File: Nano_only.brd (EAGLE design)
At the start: 53 x 20.3 mm, 3 parts

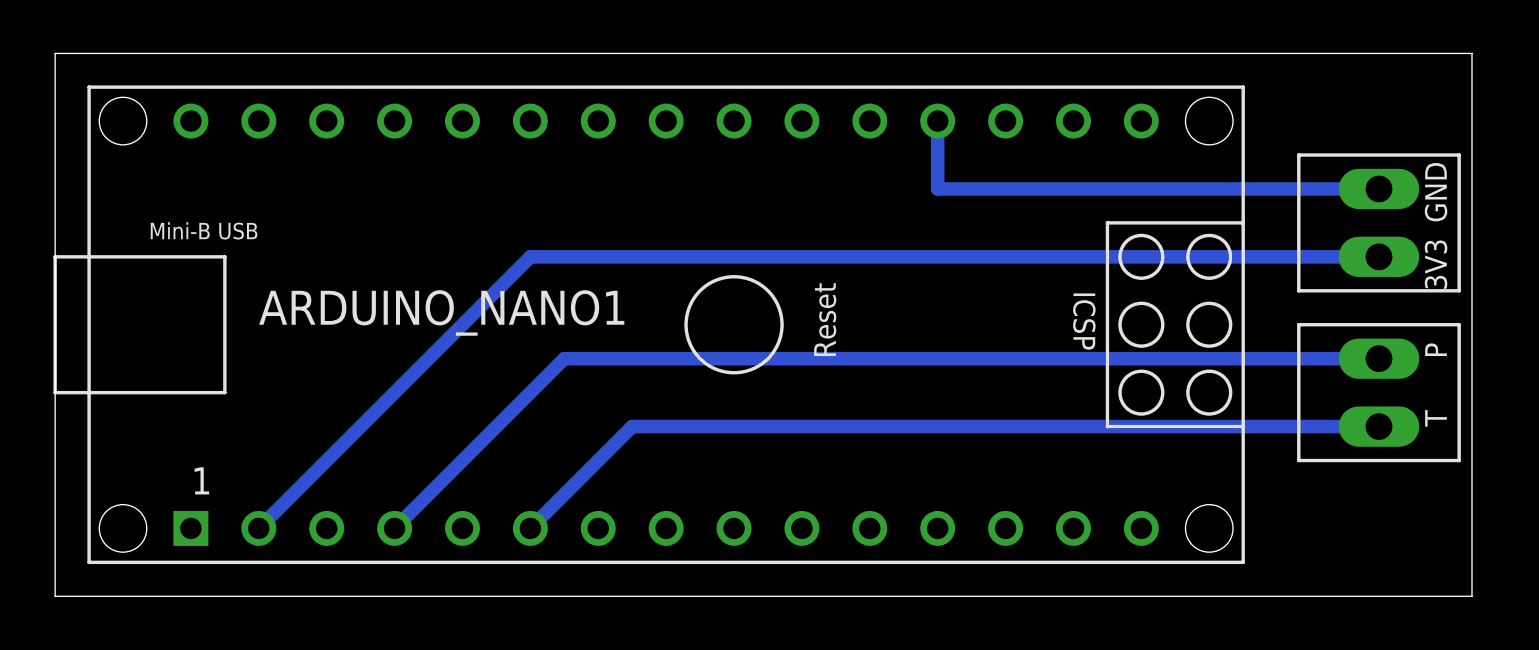
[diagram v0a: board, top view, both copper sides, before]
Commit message: Added some text on Nano_only.brd
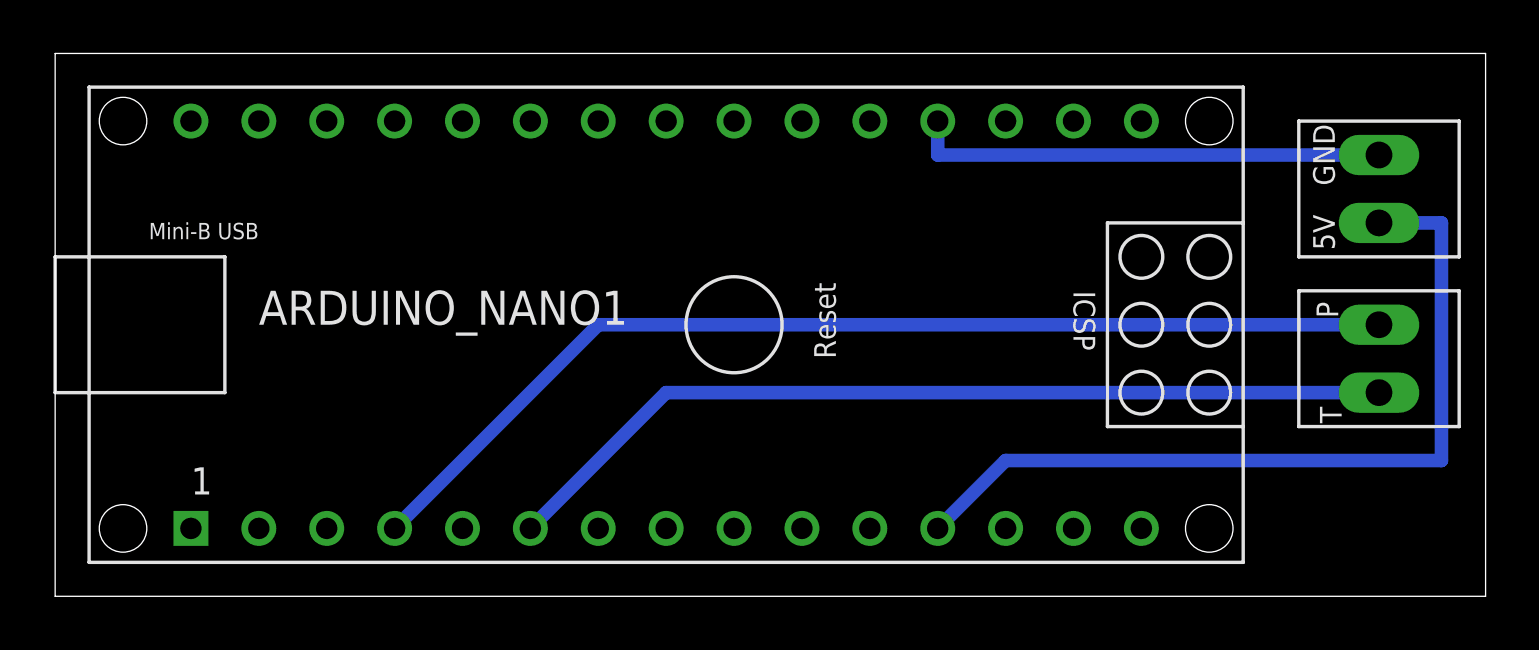
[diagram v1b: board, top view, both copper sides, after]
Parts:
- moved TPIN--PPIN 1.27 mm to (49.5, 8.89)
- moved 3.3V--GND 1.27 mm to (49.5, 15.2)
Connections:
- removed net 3V3: 3.3V--GND.P$1, ARDUINO_NANO1.2
- removed net 5V: ARDUINO_NANO1.12
- new net N$1: 3.3V--GND.P$1, ARDUINO_NANO1.12
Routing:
- net 3V3: track 46.1 -> 0.00 mm
- net N$1: track 0.00 -> 31.1 mm
- net GND: track 19.0 -> 17.8 mm
- net TPIN: track 33.3 -> 33.9 mm
- net PPIN: track 39.4 -> 39.9 mm
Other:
- board size 53 x 20.3 mm -> 53.5 x 20.3 mm
- board text added: "5V"
- board text removed: "3V3"
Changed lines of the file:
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@@
 <board>
 <plain>
-<wire x1="0" y1="0" x2="53.01" y2="0" width="0" layer="20"/>
-<wire x1="53.01" y1="0" x2="53.01" y2="20.31" width="0" layer="20"/>
-<wire x1="53.01" y1="20.31" x2="0" y2="20.31" width="0" layer="20"/>
+<wire x1="0" y1="0" x2="53.518" y2="0" width="0" layer="20"/>
+<wire x1="53.518" y1="0" x2="53.518" y2="20.31" width="0" layer="20"/>
+<wire x1="53.518" y1="20.31" x2="0" y2="20.31" width="0" layer="20"/>
 <wire x1="0" y1="20.31" x2="0" y2="0" width="0" layer="20"/>
-<text x="52.07" y="13.97" size="0.8128" layer="25" rot="R90">GND</text>
-<text x="52.07" y="11.43" size="0.8128" layer="25" rot="R90">3V3</text>
-<text x="52.07" y="8.89" size="0.8128" layer="25" rot="R90">P</text>
-<text x="52.07" y="6.35" size="0.8128" layer="25" rot="R90">T</text>
+<text x="47.879" y="15.367" size="0.8128" layer="25" rot="R90">GND</text>
+<text x="47.879" y="12.954" size="0.8128" layer="25" rot="R90">5V</text>
+<text x="48.006" y="10.414" size="0.8128" layer="25" rot="R90">P</text>
+<text x="48.133" y="6.477" size="0.8128" layer="25" rot="R90">T</text>
 </plain>
 <attributes>
@@
 </autorouter>
 <elements>
-<element name="3.3V--GND" library="johannes" package="CONRAD567588" value="CONRAD567588-2" x="49.53" y="13.97" smashed="yes" rot="R90"/>
+<element name="3.3V--GND" library="johannes" package="CONRAD567588" value="CONRAD567588-2" x="49.53" y="15.24" smashed="yes" rot="R90"/>
 <element name="ARDUINO_NANO1" library="ArduinoNanoV30" package="ARDUINO_NANO" value="" x="25.4" y="10.16" smashed="yes">
 <attribute name="NAME" x="7.62" y="10.16" size="1.27" layer="21" font="vector"/>
 <attribute name="VALUE" x="7.62" y="7.62" size="1.27" layer="21" font="vector"/>
 </element>
-<element name="TPIN--PPIN" library="johannes" package="CONRAD567588" value="CONRAD567588-2" x="49.53" y="7.62" smashed="yes" rot="R90"/>
+<element name="TPIN--PPIN" library="johannes" package="CONRAD567588" value="CONRAD567588-2" x="49.53" y="8.89" smashed="yes" rot="R90"/>
 </elements>
 <signals>
@@
 <contactref element="ARDUINO_NANO1" pad="14"/>
 <contactref element="ARDUINO_NANO1" pad="19"/>
-<wire x1="33.02" y1="17.78" x2="33.02" y2="15.24" width="0.508" layer="16"/>
-<wire x1="33.02" y1="15.24" x2="49.53" y2="15.24" width="0.508" layer="16"/>
+<wire x1="33.02" y1="17.78" x2="33.02" y2="16.51" width="0.508" layer="16"/>
+<wire x1="33.02" y1="16.51" x2="49.53" y2="16.51" width="0.508" layer="16"/>
 <wire x1="38.1" y1="2.54" x2="33.02" y2="17.78" width="0" layer="19" extent="1-1"/>
-</signal>
-<signal name="5V">
-<contactref element="ARDUINO_NANO1" pad="12"/>
 </signal>
 <signal name="VIN">
@@
 <contactref element="ARDUINO_NANO1" pad="6"/>
 <contactref element="TPIN--PPIN" pad="P$1"/>
-<wire x1="49.53" y1="6.35" x2="21.59" y2="6.35" width="0.508" layer="16"/>
-<wire x1="21.59" y1="6.35" x2="17.78" y2="2.54" width="0.508" layer="16"/>
+<wire x1="49.53" y1="7.62" x2="22.86" y2="7.62" width="0.508" layer="16"/>
+<wire x1="22.86" y1="7.62" x2="17.78" y2="2.54" width="0.508" layer="16"/>
 </signal>
 <signal name="PPIN">
 <contactref element="ARDUINO_NANO1" pad="4"/>
 <contactref element="TPIN--PPIN" pad="P$2"/>
-<wire x1="49.53" y1="8.89" x2="19.05" y2="8.89" width="0.508" layer="16"/>
-<wire x1="19.05" y1="8.89" x2="12.8016" y2="2.6416" width="0.508" layer="16"/>
+<wire x1="49.53" y1="10.16" x2="20.32" y2="10.16" width="0.508" layer="16"/>
+<wire x1="20.32" y1="10.16" x2="12.8016" y2="2.6416" width="0.508" layer="16"/>
 <wire x1="12.8016" y1="2.6416" x2="12.8016" y2="2.5908" width="0.254" layer="16"/>
 <wire x1="12.8016" y1="2.5908" x2="12.7" y2="2.54" width="0" layer="19" extent="16-16"/>
 </signal>
-<signal name="3V3">
+<signal name="N$1">
 <contactref element="3.3V--GND" pad="P$1"/>
-<contactref element="ARDUINO_NANO1" pad="2"/>
-<wire x1="49.53" y1="12.7" x2="17.78" y2="12.7" width="0.508" layer="16"/>
-<wire x1="17.78" y1="12.7" x2="7.62" y2="2.54" width="0.508" layer="16"/>
+<contactref element="ARDUINO_NANO1" pad="12"/>
+<wire x1="33.02" y1="2.54" x2="35.56" y2="5.08" width="0.508" layer="16"/>
+<wire x1="35.56" y1="5.08" x2="51.867" y2="5.08" width="0.508" layer="16"/>
+<wire x1="51.867" y1="5.08" x2="51.867" y2="13.97" width="0.508" layer="16"/>
+<wire x1="51.867" y1="13.97" x2="49.53" y2="13.97" width="0.508" layer="16"/>
 </signal>
 </signals>

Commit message: few typos, 3V3 -> 5V
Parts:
- renumbered 3.3V--GND to 5V--GND
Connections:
- net N$1 renamed 5V
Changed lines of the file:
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@@
 </autorouter>
 <elements>
-<element name="3.3V--GND" library="johannes" package="CONRAD567588" value="CONRAD567588-2" x="49.53" y="15.24" smashed="yes" rot="R90"/>
+<element name="5V--GND" library="johannes" package="CONRAD567588" value="CONRAD567588-2" x="49.53" y="15.24" smashed="yes" rot="R90"/>
 <element name="ARDUINO_NANO1" library="ArduinoNanoV30" package="ARDUINO_NANO" value="" x="25.4" y="10.16" smashed="yes">
 <attribute name="NAME" x="7.62" y="10.16" size="1.27" layer="21" font="vector"/>
@@
 <signals>
 <signal name="GND">
-<contactref element="3.3V--GND" pad="P$2"/>
+<contactref element="5V--GND" pad="P$2"/>
 <contactref element="ARDUINO_NANO1" pad="14"/>
 <contactref element="ARDUINO_NANO1" pad="19"/>
@@
 <wire x1="12.8016" y1="2.5908" x2="12.7" y2="2.54" width="0" layer="19" extent="16-16"/>
 </signal>
-<signal name="N$1">
-<contactref element="3.3V--GND" pad="P$1"/>
+<signal name="5V">
+<contactref element="5V--GND" pad="P$1"/>
 <contactref element="ARDUINO_NANO1" pad="12"/>
 <wire x1="33.02" y1="2.54" x2="35.56" y2="5.08" width="0.508" layer="16"/>
